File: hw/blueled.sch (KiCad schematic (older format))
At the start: 56 parts, among them J1 Barrel_Jack, J2 LED Strip, J3 ICSP, J4 Screw_Terminal_01x02, Q1 Q_PMOS_SDG, Q2 Q_PNP_EBC, SW2 PUSH, U1 ATmega328P-AU, U2 HC-05, U3 AMS1117-3.3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

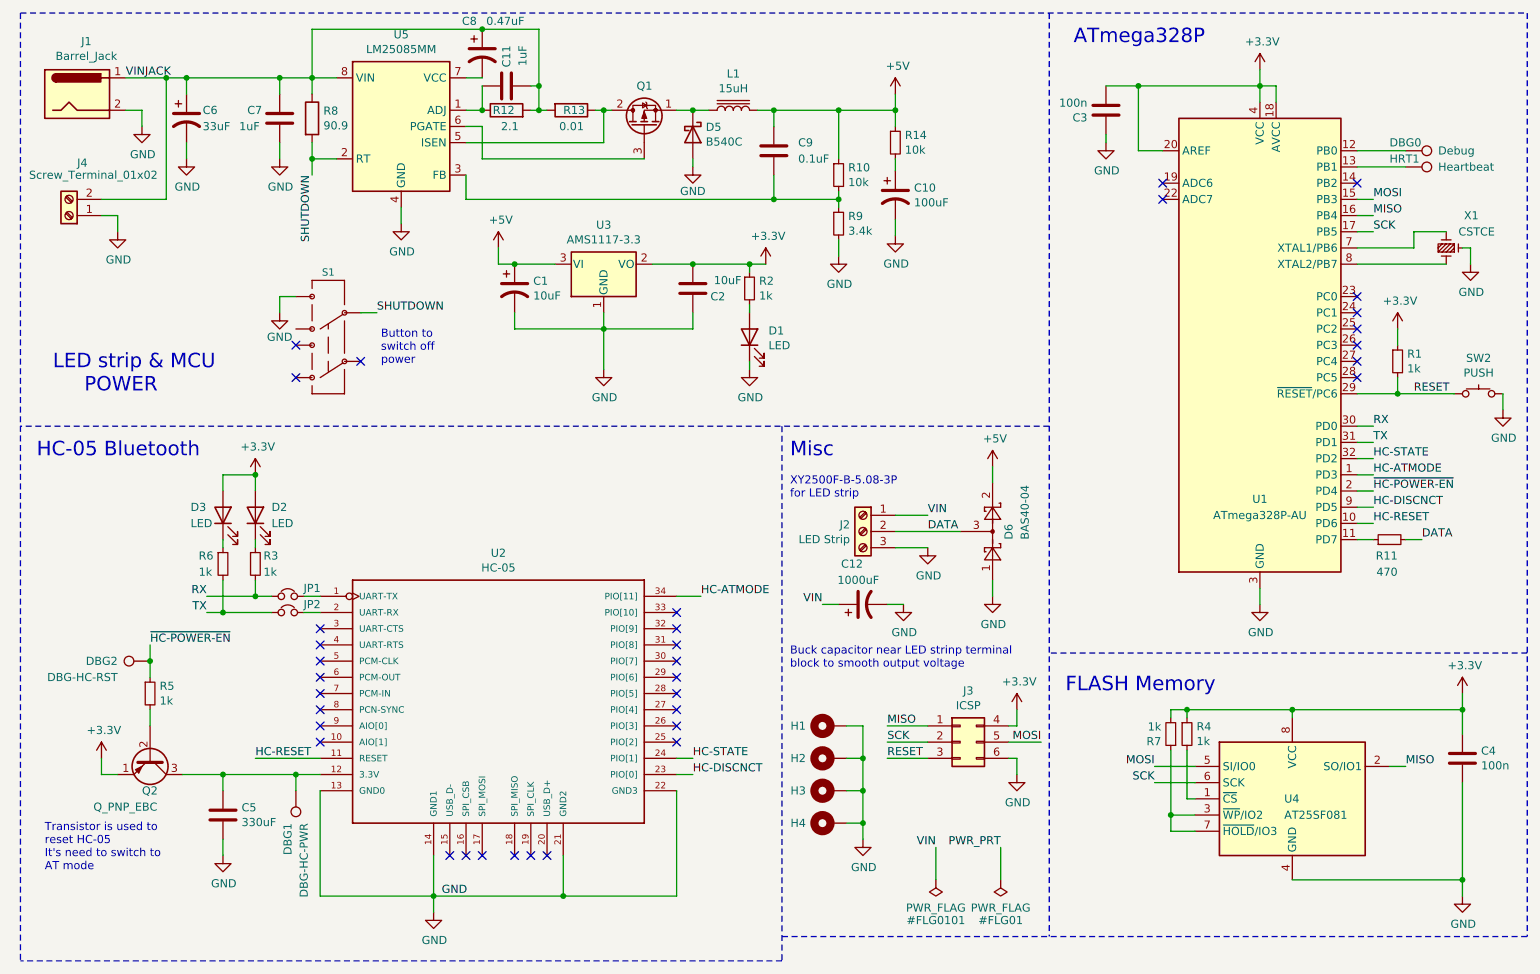
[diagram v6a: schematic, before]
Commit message: fix(hw): fix rules checker issues
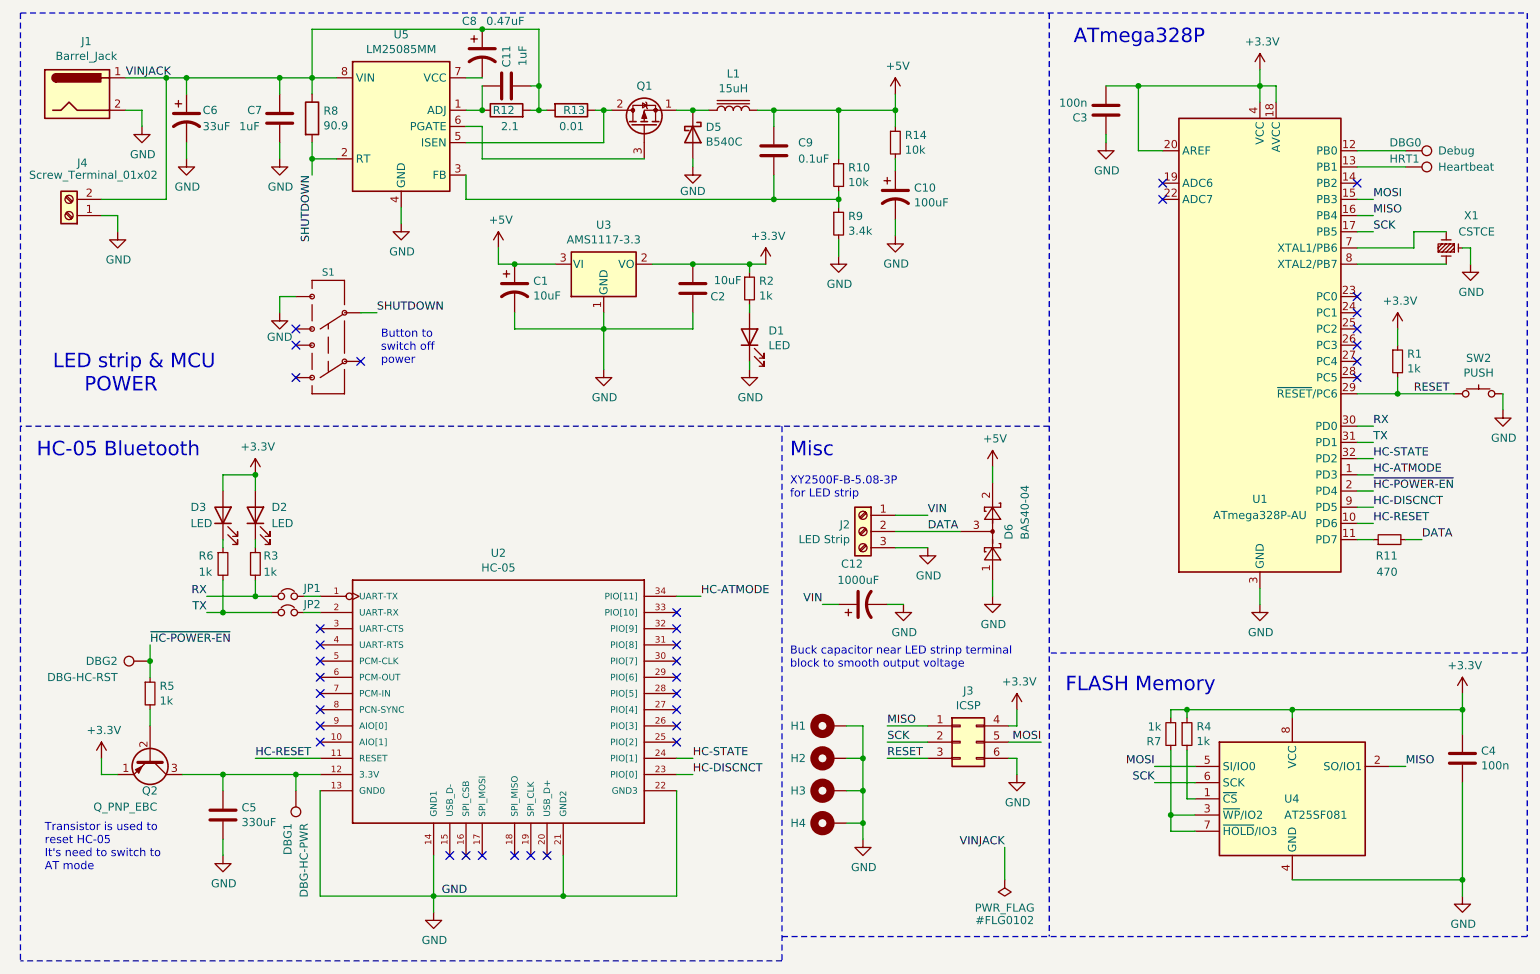
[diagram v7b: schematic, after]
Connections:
- no-connect marks 35 -> 36
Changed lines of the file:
@@
 Wire Wire Line
 	7700 5550 7700 5650
-Text Label 6250 5750 2    50   ~ 0
-VIN
-Wire Wire Line
-	6250 5950 6250 5750
-$Comp
-L power:PWR_FLAG #FLG0101
-U 1 1 5D4A1496
-P 6250 5950
-F 0 "#FLG0101" H 6250 6200 50  0000 C CNN
-F 1 "PWR_FLAG" H 6250 6123 50  0000 C CNN
-F 2 "" H 6250 5950 50  0001 C CNN
-F 3 "~" H 6250 5950 50  0001 C CNN
-	1    6250 5950
-	-1   0    0    1
-$EndComp
 $Comp
 L Device:R_Small R7
@@
 Wire Wire Line
 	1850 5300 2300 5300
-Text Label 6650 5750 2    50   ~ 0
-PWR_PRT
-Wire Wire Line
-	6650 5950 6650 5750
-$Comp
-L power:PWR_FLAG #FLG01
-U 1 1 607AA1D3
-P 6650 5950
-F 0 "#FLG01" H 6650 6200 50  0000 C CNN
-F 1 "PWR_FLAG" H 6650 6123 50  0000 C CNN
-F 2 "" H 6650 5950 50  0001 C CNN
-F 3 "~" H 6650 5950 50  0001 C CNN
-	1    6650 5950
-	-1   0    0    1
-$EndComp
 Text Notes 750  5900 0    50   ~ 0
 Transistor is used to \nreset HC-05\nIt's need to switch to \nAT mode
@@
 Text Notes 2825 2775 0    50   ~ 0
 Button to \nswitch off \npower
+NoConn ~ 2300 2550
+Text Label 6675 5750 2    50   ~ 0
+VINJACK
+Wire Wire Line
+	6675 5950 6675 5750
+$Comp
+L power:PWR_FLAG #FLG0102
+U 1 1 5FD3734B
+P 6675 5950
+F 0 "#FLG0102" H 6675 6200 50  0000 C CNN
+F 1 "PWR_FLAG" H 6675 6123 50  0000 C CNN
+F 2 "" H 6675 5950 50  0001 C CNN
+F 3 "~" H 6675 5950 50  0001 C CNN
+	1    6675 5950
+	-1   0    0    1
+$EndComp
 $EndSCHEMATC

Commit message: add(hw): BOM updates
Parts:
- H1, H2, H3, H4: footprint (none) -> MountingHole:MountingHole_3.2mm_M3
- U5: footprint Package_SO:MSOP-8_3x3mm_P0.65mm -> Package_SO:VSSOP-8_3.0x3.0mm_P0.65mm; Distributor (none) -> lcsc.com; Manuf. Part (none) -> LM25085MM/NOPB
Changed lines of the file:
@@
 F 0 "H1" V 5600 5200 50  0000 C CNN
 F 1 "MountingHole_Pad" V 5746 5003 50  0001 C CNN
-F 2 "" H 5600 5000 50  0001 C CNN
+F 2 "MountingHole:MountingHole_3.2mm_M3" H 5600 5000 50  0001 C CNN
 F 3 "~" H 5600 5000 50  0001 C CNN
 	1    5600 5000
@@
 F 0 "H2" V 5600 5400 50  0000 C CNN
 F 1 "MountingHole_Pad" V 5746 5203 50  0001 C CNN
-F 2 "" H 5600 5200 50  0001 C CNN
+F 2 "MountingHole:MountingHole_3.2mm_M3" H 5600 5200 50  0001 C CNN
 F 3 "~" H 5600 5200 50  0001 C CNN
 	1    5600 5200
@@
 F 0 "H3" V 5600 5600 50  0000 C CNN
 F 1 "MountingHole_Pad" V 5746 5403 50  0001 C CNN
-F 2 "" H 5600 5400 50  0001 C CNN
+F 2 "MountingHole:MountingHole_3.2mm_M3" H 5600 5400 50  0001 C CNN
 F 3 "~" H 5600 5400 50  0001 C CNN
 	1    5600 5400
@@
 F 0 "H4" V 5600 5800 50  0000 C CNN
 F 1 "MountingHole_Pad" V 5746 5603 50  0001 C CNN
-F 2 "" H 5600 5600 50  0001 C CNN
+F 2 "MountingHole:MountingHole_3.2mm_M3" H 5600 5600 50  0001 C CNN
 F 3 "~" H 5600 5600 50  0001 C CNN
 	1    5600 5600
@@
 F 0 "U5" H 2950 1867 50  0000 C CNN
 F 1 "LM25085MM" H 2950 1776 50  0000 C CNN
-F 2 "Package_SO:MSOP-8_3x3mm_P0.65mm" H 3000 850 50  0001 L CIN
+F 2 "Package_SO:VSSOP-8_3.0x3.0mm_P0.65mm" H 3000 850 50  0001 L CIN
 F 3 "http://www.ti.com/lit/ds/symlink/lm25085.pdf" H 2950 1300 50  0001 C CNN
+F 4 "lcsc.com" H 2950 1300 50  0001 C CNN "Distributor"
+F 5 "LM25085MM/NOPB" H 2950 1300 50  0001 C CNN "Manuf. Part"
 	1    2950 1300
 	1    0    0    -1
